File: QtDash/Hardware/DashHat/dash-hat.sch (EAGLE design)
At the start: 156 parts, among them IC1 LM324, IC2 MCP3X083008, IC3 MCP23017SS, IC4 LM358D, IC5 IL300, IC6 LM358D, IC7 IL300, IC8 LM358D, IC9 DS1374, J1 CONN_20X2, J10 455-1750-1-ND, J11 455-1750-1-ND, J15 455-1750-1-ND, J6 VOLVO_CONN_31, J7 VOLVO_CONN_32, J8 455-1750-1-ND, J9 455-1750-1-ND, Y1 ECX-.327-6-34RR

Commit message: - finished adding yageo resistors to schematic -- should all of the right part numbers now 	- TODO: caps
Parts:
- R1, R4, R57, R58, R6, R65, R69, R8: value 100 -> 100R; device SparkFun-Resistors:100OHM-0603-1/10W-1% -> digital_dash:RC0603JR-07100RL
- R10, R11, R12, R63, R67, R75, R9: device SparkFun-Resistors:1KOHM-0603-1/10W-1% -> digital_dash:RC0603JR-071KL
- R13, R14, R15, R16, R66, R70: value 640k -> 620k; device SparkFun-Resistors:390KOHM-0603-1/10W-1% -> digital_dash:RC0603JR-07620KL
- R17, R18, R19, R20, R21, R22, R23, R24, R25, R26, R27, R28, R29, R30, R31, R32, R33, R34, R35, R36, R37, R38, R39, R40, R41, R42, R43, R44, R45, R46, R47, R48, R49, R50, R51, R52: value 470 -> 470R; device SparkFun-Resistors:470OHM-0603-1/10W-1% -> digital_dash:RC0603JR-07470RL
- R2, R3, R5, R64, R68, R7: device SparkFun-Resistors:330KOHM-0603-1/10W-1% -> digital_dash:RC0603JR-07330KL
- R53, R54, R59, R60: device SparkFun-Resistors:1MOHM-0603-1/4W-5% -> digital_dash:RC0603JR-071ML
- R55, R61: value 10 -> 10R; device SparkFun-Resistors:10OHM-0603-1/10W-5% -> digital_dash:RC0603JR-1310RL
- R56, R62, R71, R72, R73, R74: device SparkFun-Resistors:100KOHM-0603-1/10W-1% -> digital_dash:RC0603JR-07100KL
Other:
- moved on the sheet: C11, C14

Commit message: - added real part numbers for capacitors 	- made new BOM/parts list
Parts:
- C1, C17, C18, C2, C3, C4: value 10nF -> 10n; device SparkFun-Capacitors:10NF-0603-50V-10% -> digital_dash:CL10B103KB8NNNC
- C10, C13, C14, C16, C20, C6, C8: value 1.0uF -> 1u; device SparkFun-Capacitors:1.0UF-0603-16V-10% -> digital_dash:CL10A105KA8NNNC
- C11, C12, C15, C19, C5, C7, C9: value 0.1uF -> 100n; device SparkFun-Capacitors:0.1UF-0603-25V-5% -> digital_dash:CL10B104MB8NNNC
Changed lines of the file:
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@@
 <setting verticaltext="up"/>
 </settings>
-<grid distance="0.05" unitdist="inch" unit="inch" style="lines" multiple="1" display="no" altdistance="0.01" altunitdist="inch" altunit="inch"/>
+<grid distance="0.1" unitdist="inch" unit="inch" style="lines" multiple="1" display="no" altdistance="0.01" altunitdist="inch" altunit="inch"/>
 <layers>
 <layer number="1" name="Top" color="4" fill="1" visible="no" active="no"/>
@@
 <part name="IC1" library="digital_dash" deviceset="LM324" device=""/>
 <part name="R2" library="digital_dash" deviceset="RC0603JR" device="" technology="-07330KL" value="330k"/>
-<part name="C1" library="SparkFun-Capacitors" deviceset="10NF" device="-0603-50V-10%" value="10nF"/>
+<part name="C1" library="digital_dash" deviceset="CL" device="" technology="10B103KB8NNNC" value="10n"/>
 <part name="GND1" library="SparkFun-PowerSymbols" deviceset="GND" device=""/>
 <part name="SUPPLY1" library="SparkFun-PowerSymbols" deviceset="5V" device=""/>
 <part name="GND5" library="SparkFun-PowerSymbols" deviceset="GND" device=""/>
-<part name="C5" library="SparkFun-Capacitors" deviceset="0.1UF" device="-0603-25V-5%" value="0.1uF"/>
+<part name="C5" library="digital_dash" deviceset="CL" device="" technology="10B104MB8NNNC" value="100n"/>
 <part name="GND6" library="SparkFun-PowerSymbols" deviceset="GND" device=""/>
 <part name="J2" library="SparkFun-Connectors" deviceset="CONN_02" device=""/>
@@
 <part name="GND2" library="SparkFun-PowerSymbols" deviceset="GND" device=""/>
 <part name="R3" library="digital_dash" deviceset="RC0603JR" device="" technology="-07330KL" value="330k"/>
-<part name="C2" library="SparkFun-Capacitors" deviceset="10NF" device="-0603-50V-10%" value="10nF"/>
+<part name="C2" library="digital_dash" deviceset="CL" device="" technology="10B103KB8NNNC" value="10n"/>
 <part name="GND3" library="SparkFun-PowerSymbols" deviceset="GND" device=""/>
 <part name="R4" library="digital_dash" deviceset="RC0603JR" device="" technology="-07100RL" value="100R"/>
@@
 <part name="GND4" library="SparkFun-PowerSymbols" deviceset="GND" device=""/>
 <part name="R5" library="digital_dash" deviceset="RC0603JR" device="" technology="-07330KL" value="330k"/>
-<part name="C3" library="SparkFun-Capacitors" deviceset="10NF" device="-0603-50V-10%" value="10nF"/>
+<part name="C3" library="digital_dash" deviceset="CL" device="" technology="10B103KB8NNNC" value="10n"/>
 <part name="GND11" library="SparkFun-PowerSymbols" deviceset="GND" device=""/>
 <part name="R6" library="digital_dash" deviceset="RC0603JR" device="" technology="-07100RL" value="100R"/>
@@
 <part name="GND12" library="SparkFun-PowerSymbols" deviceset="GND" device=""/>
 <part name="R7" library="digital_dash" deviceset="RC0603JR" device="" technology="-07330KL" value="330k"/>
-<part name="C4" library="SparkFun-Capacitors" deviceset="10NF" device="-0603-50V-10%" value="10nF"/>
+<part name="C4" library="digital_dash" deviceset="CL" device="" technology="10B103KB8NNNC" value="10n"/>
 <part name="GND13" library="SparkFun-PowerSymbols" deviceset="GND" device=""/>
 <part name="R8" library="digital_dash" deviceset="RC0603JR" device="" technology="-07100RL" value="100R"/>
@@
 <part name="IC2" library="digital_dash" deviceset="MCP3X08" device="3008"/>
 <part name="SUPPLY12" library="SparkFun-PowerSymbols" deviceset="3.3V" device=""/>
-<part name="C6" library="SparkFun-Capacitors" deviceset="1.0UF" device="-0603-16V-10%" value="1.0uF"/>
-<part name="C7" library="SparkFun-Capacitors" deviceset="0.1UF" device="-0603-25V-5%" value="0.1uF"/>
+<part name="C6" library="digital_dash" deviceset="CL" device="" technology="10A105KA8NNNC" value="1u"/>
+<part name="C7" library="digital_dash" deviceset="CL" device="" technology="10B104MB8NNNC" value="100n"/>
 <part name="GND21" library="SparkFun-PowerSymbols" deviceset="GND" device=""/>
-<part name="C8" library="SparkFun-Capacitors" deviceset="1.0UF" device="-0603-16V-10%" value="1.0uF"/>
+<part name="C8" library="digital_dash" deviceset="CL" device="" technology="10A105KA8NNNC" value="1u"/>
 <part name="GND22" library="SparkFun-PowerSymbols" deviceset="GND" device=""/>
 <part name="IC3" library="microchip" deviceset="MCP23017" device="SS" value="MCP23017SS"/>
@@
 <part name="GND39" library="SparkFun-PowerSymbols" deviceset="GND" device=""/>
 <part name="SUPPLY29" library="SparkFun-PowerSymbols" deviceset="3.3V" device=""/>
-<part name="C9" library="SparkFun-Capacitors" deviceset="0.1UF" device="-0603-25V-5%" value="0.1uF"/>
+<part name="C9" library="digital_dash" deviceset="CL" device="" technology="10B104MB8NNNC" value="100n"/>
 <part name="GND40" library="SparkFun-PowerSymbols" deviceset="GND" device=""/>
-<part name="C10" library="SparkFun-Capacitors" deviceset="1.0UF" device="-0603-16V-10%" value="1.0uF"/>
+<part name="C10" library="digital_dash" deviceset="CL" device="" technology="10A105KA8NNNC" value="1u"/>
 <part name="OK3" library="digital_dash" deviceset="ILQ1" device="X009"/>
 <part name="R41" library="digital_dash" deviceset="RC0603JR" device="" technology="-07470RL" value="470R"/>
@@
 <part name="SUPPLY37" library="SparkFun-PowerSymbols" deviceset="3.3V" device=""/>
 <part name="GND48" library="SparkFun-PowerSymbols" deviceset="GND" device=""/>
-<part name="C12" library="SparkFun-Capacitors" deviceset="0.1UF" device="-0603-25V-5%" value="0.1uF"/>
-<part name="C13" library="SparkFun-Capacitors" deviceset="1.0UF" device="-0603-16V-10%" value="1.0uF"/>
+<part name="C12" library="digital_dash" deviceset="CL" device="" technology="10B104MB8NNNC" value="100n"/>
+<part name="C13" library="digital_dash" deviceset="CL" device="" technology="10A105KA8NNNC" value="1u"/>
 <part name="R57" library="digital_dash" deviceset="RC0603JR" device="" technology="-07100RL" value="100R"/>
 <part name="SUPPLY40" library="SparkFun-PowerSymbols" deviceset="12V" device=""/>
@@
 <part name="IC6" library="digital_dash" deviceset="LM358" device="D"/>
 <part name="GND56" library="SparkFun-PowerSymbols" deviceset="GND" device=""/>
-<part name="C11" library="SparkFun-Capacitors" deviceset="0.1UF" device="-0603-25V-5%" value="0.1uF"/>
-<part name="C14" library="SparkFun-Capacitors" deviceset="1.0UF" device="-0603-16V-10%" value="1.0uF"/>
+<part name="C11" library="digital_dash" deviceset="CL" device="" technology="10B104MB8NNNC" value="100n"/>
+<part name="C14" library="digital_dash" deviceset="CL" device="" technology="10A105KA8NNNC" value="1u"/>
 <part name="SUPPLY42" library="SparkFun-PowerSymbols" deviceset="3.3V" device=""/>
 <part name="GND57" library="SparkFun-PowerSymbols" deviceset="GND" device=""/>
@@
 <part name="GND25" library="SparkFun-PowerSymbols" deviceset="GND" device=""/>
 <part name="SUPPLY44" library="SparkFun-PowerSymbols" deviceset="5V" device=""/>
-<part name="C15" library="SparkFun-Capacitors" deviceset="0.1UF" device="-0603-25V-5%" value="0.1uF"/>
+<part name="C15" library="digital_dash" deviceset="CL" device="" technology="10B104MB8NNNC" value="100n"/>
 <part name="GND27" library="SparkFun-PowerSymbols" deviceset="GND" device=""/>
-<part name="C16" library="SparkFun-Capacitors" deviceset="1.0UF" device="-0603-16V-10%" value="1.0uF"/>
+<part name="C16" library="digital_dash" deviceset="CL" device="" technology="10A105KA8NNNC" value="1u"/>
 <part name="R63" library="digital_dash" deviceset="RC0603JR" device="" technology="-071KL" value="1k"/>
 <part name="SUPPLY45" library="SparkFun-PowerSymbols" deviceset="5V" device=""/>
 <part name="R64" library="digital_dash" deviceset="RC0603JR" device="" technology="-07330KL" value="330k"/>
-<part name="C17" library="SparkFun-Capacitors" deviceset="10NF" device="-0603-50V-10%" value="10nF"/>
+<part name="C17" library="digital_dash" deviceset="CL" device="" technology="10B103KB8NNNC" value="10n"/>
 <part name="GND28" library="SparkFun-PowerSymbols" deviceset="GND" device=""/>
 <part name="R65" library="digital_dash" deviceset="RC0603JR" device="" technology="-07100RL" value="100R"/>
@@
 <part name="SUPPLY47" library="SparkFun-PowerSymbols" deviceset="5V" device=""/>
 <part name="R68" library="digital_dash" deviceset="RC0603JR" device="" technology="-07330KL" value="330k"/>
-<part name="C18" library="SparkFun-Capacitors" deviceset="10NF" device="-0603-50V-10%" value="10nF"/>
+<part name="C18" library="digital_dash" deviceset="CL" device="" technology="10B103KB8NNNC" value="10n"/>
 <part name="GND36" library="SparkFun-PowerSymbols" deviceset="GND" device=""/>
 <part name="R69" library="digital_dash" deviceset="RC0603JR" device="" technology="-07100RL" value="100R"/>
@@
 <part name="GND46" library="SparkFun-PowerSymbols" deviceset="GND" device=""/>
 <part name="SUPPLY53" library="SparkFun-PowerSymbols" deviceset="3.3V" device=""/>
-<part name="C19" library="SparkFun-Capacitors" deviceset="0.1UF" device="-0603-25V-5%" value="0.1uF"/>
+<part name="C19" library="digital_dash" deviceset="CL" device="" technology="10B104MB8NNNC" value="100n"/>
 <part name="GND49" library="SparkFun-PowerSymbols" deviceset="GND" device=""/>
-<part name="C20" library="SparkFun-Capacitors" deviceset="1.0UF" device="-0603-16V-10%" value="1.0uF"/>
+<part name="C20" library="digital_dash" deviceset="CL" device="" technology="10A105KA8NNNC" value="1u"/>
 <part name="R75" library="digital_dash" deviceset="RC0603JR" device="" technology="-071KL" value="1k"/>
 <part name="SUPPLY54" library="SparkFun-PowerSymbols" deviceset="3.3V" device=""/>

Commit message: - added load resistor to alternator D+ connection -- not sure what kind of current is needed for this -- 15 Ohm 5W EP5WS15RJ 17.5mm axial resistor spec'd for now
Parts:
- added J16: TACH_IN, SparkFun-Connectors:CONN_03
- added JP24: TACH_INPUT_SEL, SparkFun-Jumpers:JUMPER-SMT_3_NO_SILK
- added R76, R77, R78, R79: 1k, digital_dash:RC0603JR-071KL
- added R82: (no value), resistor:R-US_0617/17
- J15: value 455-1750-1-ND -> VSS_IN
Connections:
- new net GPIO13: J1.33, JP24.3
- new net GPIO19: J1.35, JP23.1
- new net GPIO26: J1.37, JP23.3
- new net GPIO6: J1.31, JP24.1
- new net N$43: J16.2, JP24.2, R76.1, R77.2
- net 12V: now also R82.2
- net 3.3V: now also J16.3, R76.2, R78.2
- net CHARGING_N: now also R82.1
- net GND: now also J16.1, R77.1, R79.1
- net GPIO17: no longer JP23.1
- net GPIO27: no longer JP23.3
- net N$33: now also R78.1, R79.2
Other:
- moved on the sheet: J15, JP23

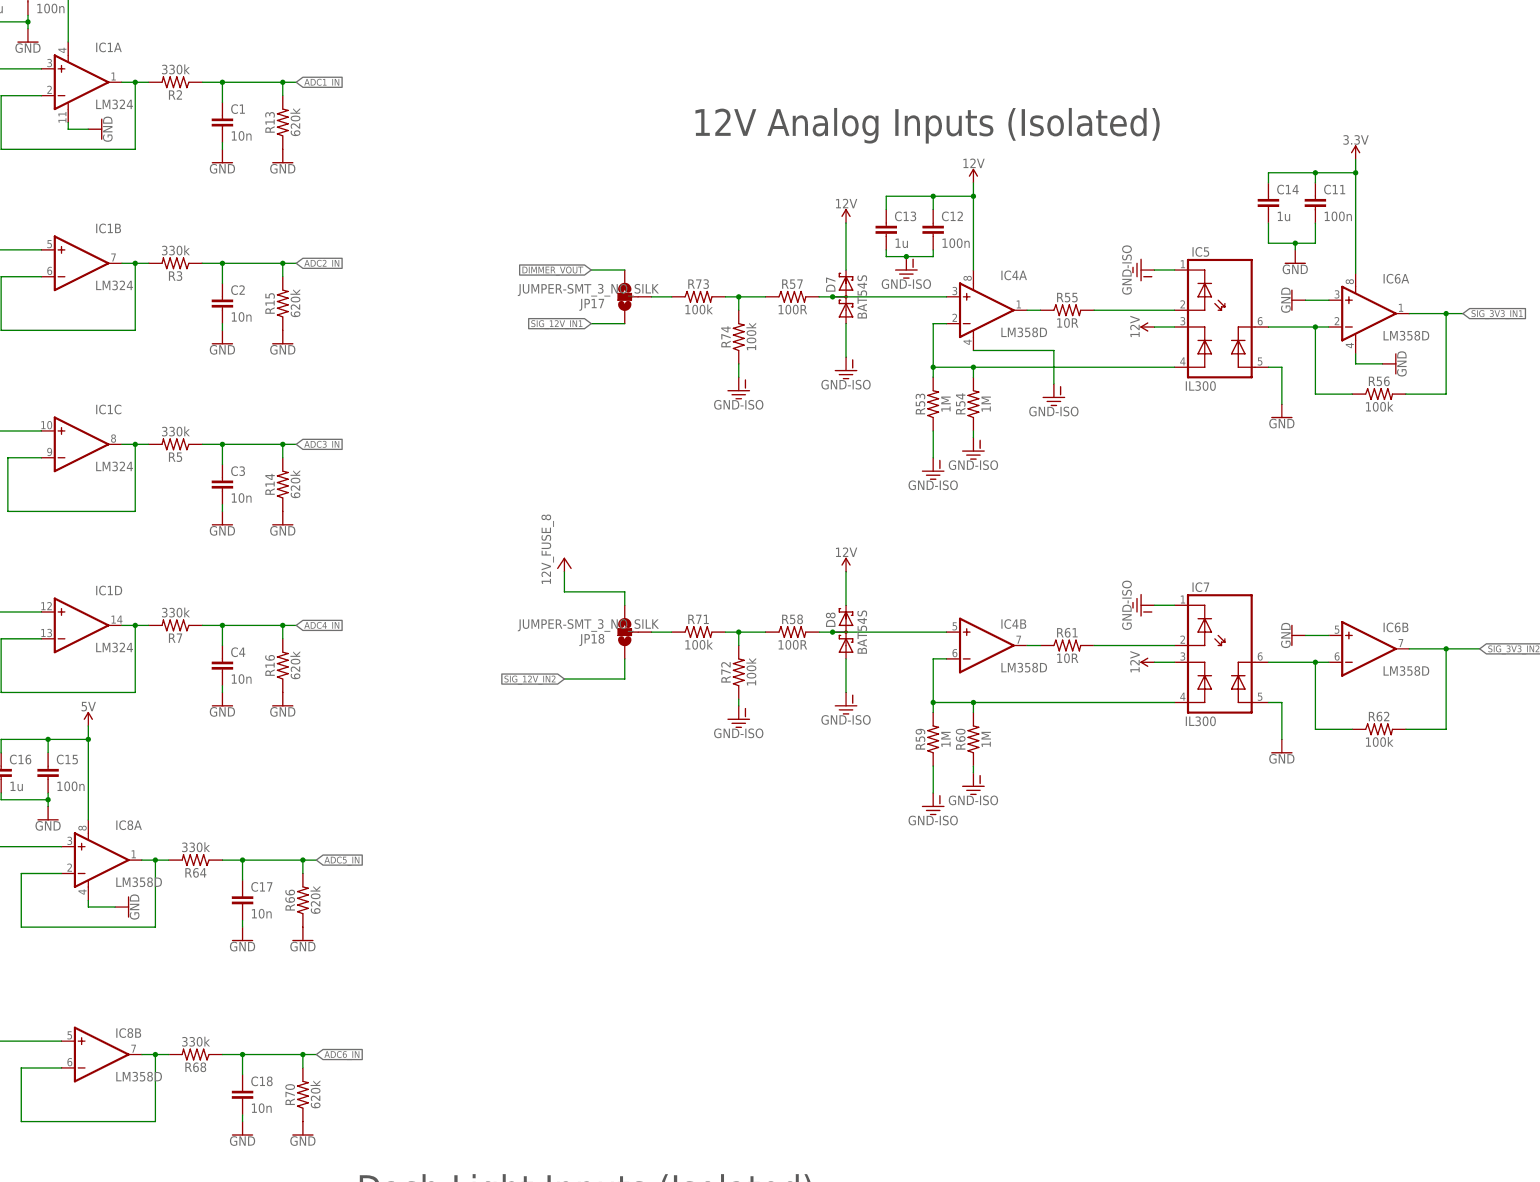
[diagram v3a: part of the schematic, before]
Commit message: bugfix/hardware-revA-issues: 	- updated library to include TSV912 and LMV614 (RRIO -- what should have been in there to begin with) 	- made room for ethernet port 	- added ground planes where available in middle layers 	- moved traces away from mounting holes
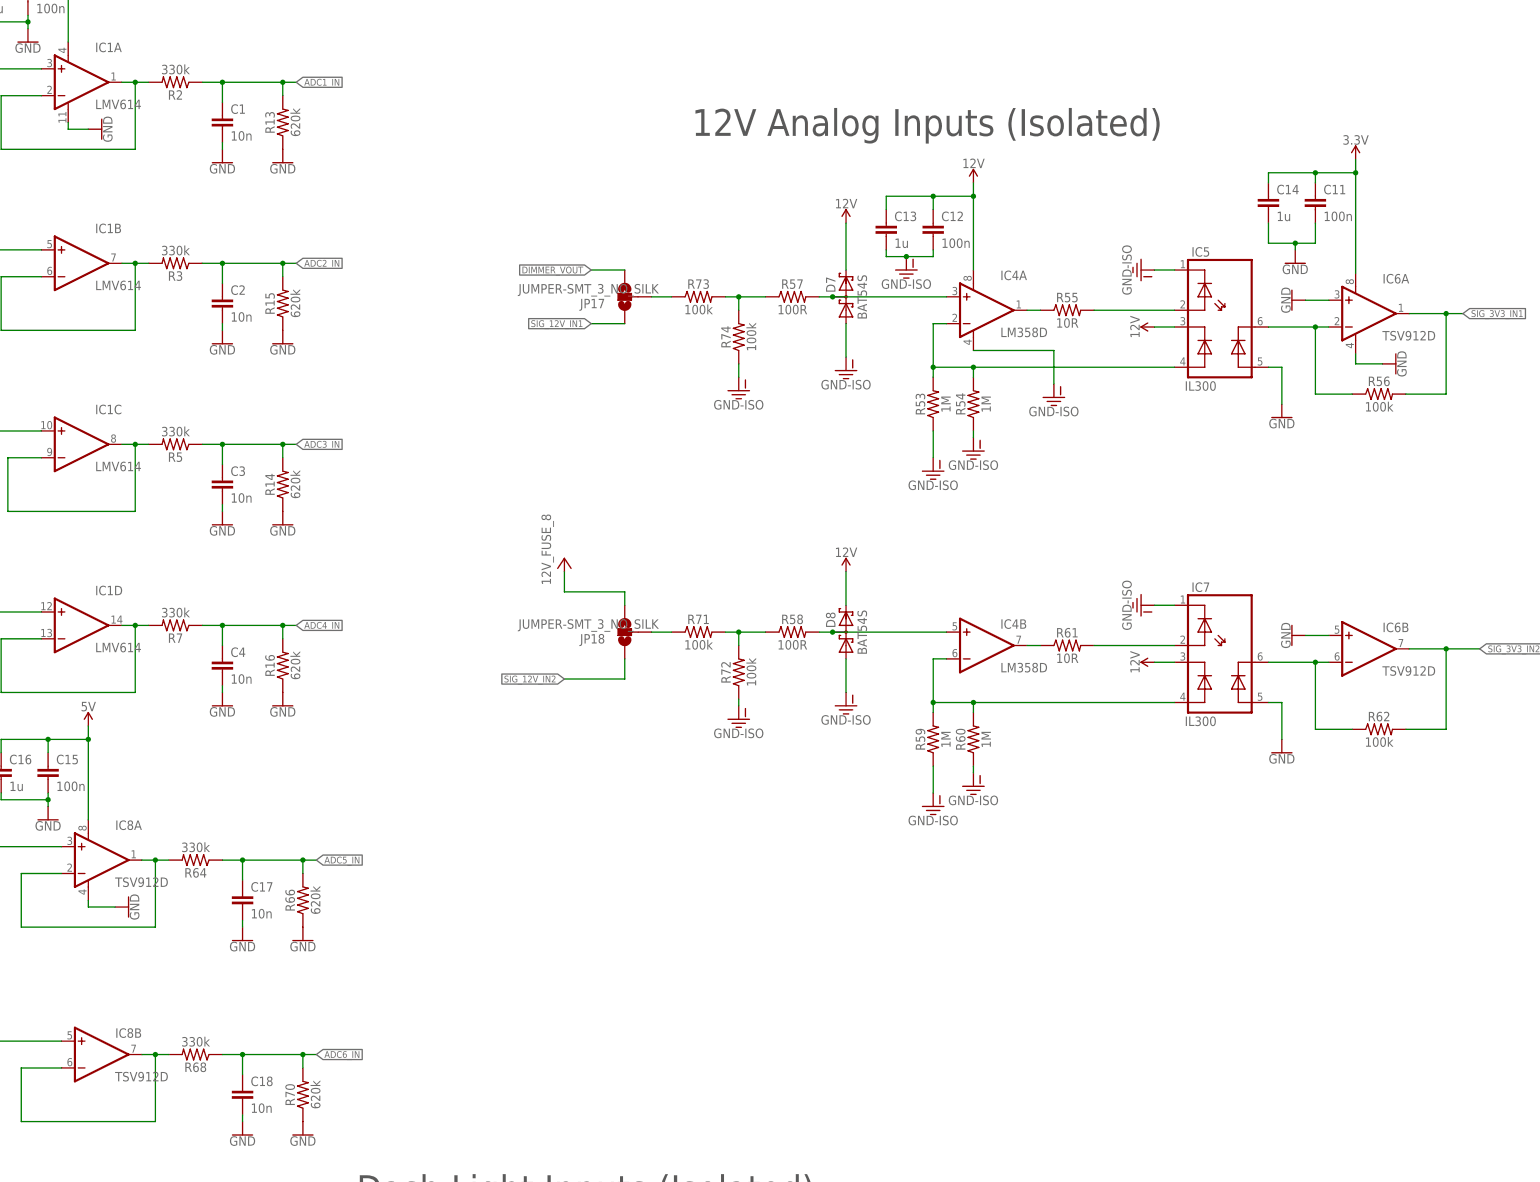
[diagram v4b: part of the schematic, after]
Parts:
- IC1: value LM324 -> LMV614; device digital_dash:LM324 -> digital_dash:LMV614
- IC6, IC8: value LM358D -> TSV912D; device digital_dash:LM358D -> digital_dash:TSV912D
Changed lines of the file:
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@@
 <setting verticaltext="up"/>
 </settings>
-<grid distance="0.05" unitdist="inch" unit="inch" style="lines" multiple="1" display="no" altdistance="0.01" altunitdist="inch" altunit="inch"/>
+<grid distance="0.1" unitdist="inch" unit="inch" style="lines" multiple="1" display="no" altdistance="0.01" altunitdist="inch" altunit="inch"/>
 <layers>
 <layer number="1" name="Top" color="4" fill="1" visible="no" active="no"/>
@@
 <parts>
 <part name="J1" library="SparkFun-Connectors" deviceset="CONN_20X2" device=""/>
-<part name="IC1" library="digital_dash" deviceset="LM324" device=""/>
+<part name="IC1" library="digital_dash" deviceset="LMV614" device=""/>
 <part name="R2" library="digital_dash" deviceset="RC0603JR" device="" technology="-07330KL" value="330k"/>
 <part name="C1" library="digital_dash" deviceset="CL" device="" technology="10B103KB8NNNC" value="10n"/>
@@
 <part name="GND55" library="SparkFun-PowerSymbols" deviceset="GND" device=""/>
 <part name="R56" library="digital_dash" deviceset="RC0603JR" device="" technology="-07100KL" value="100k"/>
-<part name="IC6" library="digital_dash" deviceset="LM358" device="D"/>
+<part name="IC6" library="digital_dash" deviceset="TSV912" device="D"/>
 <part name="GND56" library="SparkFun-PowerSymbols" deviceset="GND" device=""/>
 <part name="C11" library="digital_dash" deviceset="CL" device="" technology="10B104MB8NNNC" value="100n"/>
@@
 <part name="GND-ISO23" library="SparkFun-PowerSymbols" deviceset="GND-ISO" device=""/>
 <part name="U$3" library="digital_dash" deviceset="12V_FUSE_8" device=""/>
-<part name="IC8" library="digital_dash" deviceset="LM358" device="D"/>
+<part name="IC8" library="digital_dash" deviceset="TSV912" device="D"/>
 <part name="GND23" library="SparkFun-PowerSymbols" deviceset="GND" device=""/>
 <part name="GND25" library="SparkFun-PowerSymbols" deviceset="GND" device=""/>
